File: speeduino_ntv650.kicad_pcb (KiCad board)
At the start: 2 copper layers, 0 parts

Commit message: first routing
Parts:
- added A1: Pololu_Breakout_A4988, ntv650_ecu:A4988 Stepper Motor Driver Carrier, B.Cu at (74.3, 77.5)
- added ARD1: ArduinoMegaProMini, ntv650_ecu:ArduinoMegaProMini, F.Cu at (117.0, 111.0)
- added C1: 0.01mF, Capacitors_ThroughHole:C_Axial_L5.1mm_D3.1mm_P7.50mm_Horizontal, B.Cu at (134.6, 86.4)
- added C10: 0.22uF, Capacitors_ThroughHole:C_Axial_L5.1mm_D3.1mm_P7.50mm_Horizontal, F.Cu at (109.0, 78.0)
- added C11: 0.1uF, Capacitors_ThroughHole:C_Axial_L5.1mm_D3.1mm_P7.50mm_Horizontal, B.Cu at (80.0, 57.8)
- added C12: 0.22uF, Capacitors_ThroughHole:C_Axial_L5.1mm_D3.1mm_P7.50mm_Horizontal, F.Cu at (121.9, 73.0)
- added C13: 0.1uF, Capacitors_ThroughHole:C_Axial_L5.1mm_D3.1mm_P7.50mm_Horizontal, F.Cu at (134.0, 97.0)
- added C14: 0.22uF, Capacitors_ThroughHole:C_Axial_L5.1mm_D3.1mm_P7.50mm_Horizontal, B.Cu at (140.3, 102.2)
- added C15: 0.1uF, Capacitors_ThroughHole:C_Axial_L5.1mm_D3.1mm_P7.50mm_Horizontal, F.Cu at (101.0, 58.4)
- added C16: 0.22uF, Capacitors_ThroughHole:C_Axial_L5.1mm_D3.1mm_P7.50mm_Horizontal, F.Cu at (117.0, 94.0)
- added C17: 1uF, Capacitors_ThroughHole:C_Axial_L5.1mm_D3.1mm_P7.50mm_Horizontal, F.Cu at (128.0, 38.0)
- added C18: 10uF, Capacitors_ThroughHole:C_Axial_L5.1mm_D3.1mm_P7.50mm_Horizontal, F.Cu at (85.0, 35.0)
- added C19: 0.1uF, Capacitors_ThroughHole:C_Axial_L5.1mm_D3.1mm_P7.50mm_Horizontal, F.Cu at (86.0, 50.0)
- added C2: 1nF, Capacitors_ThroughHole:C_Axial_L5.1mm_D3.1mm_P7.50mm_Horizontal, B.Cu at (151.8, 69.3)
- added C3: 1nF, Capacitors_ThroughHole:C_Axial_L5.1mm_D3.1mm_P7.50mm_Horizontal, F.Cu at (151.8, 88.3)
- added C4: 0.3uF, Capacitors_ThroughHole:C_Axial_L5.1mm_D3.1mm_P7.50mm_Horizontal, F.Cu at (134.0, 54.0)
- added C5: 1uF, Capacitors_ThroughHole:C_Axial_L5.1mm_D3.1mm_P7.50mm_Horizontal, F.Cu at (121.3, 58.4)
- added C6: 0.01uF, Capacitors_ThroughHole:C_Axial_L5.1mm_D3.1mm_P7.50mm_Horizontal, F.Cu at (128.3, 58.4)
- added C7: 0.1uF, Capacitors_ThroughHole:C_Axial_L5.1mm_D3.1mm_P7.50mm_Horizontal, F.Cu at (111.8, 58.4)
- added C8: 0.22uF, Capacitors_ThroughHole:C_Axial_L5.1mm_D3.1mm_P7.50mm_Horizontal, F.Cu at (117.0, 88.0)
- added C9: 0.1uF, Capacitors_ThroughHole:C_Axial_L5.1mm_D3.1mm_P7.50mm_Horizontal, F.Cu at (94.6, 58.4)
- added D1: LED, LEDs:LED_0805, F.Cu at (141.6, 18.4)
- added D2: D, Diodes_SMD:D_0805, F.Cu at (79.4, 17.1)
- added D3: LED, LEDs:LED_0805, F.Cu at (149.0, 35.0)
- added D4: D, Diodes_SMD:D_0805, F.Cu at (146.0, 28.0)
- added D5: LED, LEDs:LED_0805, F.Cu at (133.0, 73.0)
- added D6: LED, LEDs:LED_0805, F.Cu at (104.0, 95.0)
- added D7: 1N5818, Diodes_ThroughHole:D_DO-15_P12.70mm_Horizontal, F.Cu at (69.2, 33.7)
- added D8: 1N5919BG, Diodes_ThroughHole:D_DO-15_P12.70mm_Horizontal, F.Cu at (102.2, 71.8)
- added IC1: SP721, Housings_SOIC:SOIC-8-1EP_3.9x4.9mm_Pitch1.27mm, F.Cu at (111.7, 92.0)
- added IC2: TC4424, Housings_SOIC:SOIC-16W_7.5x10.3mm_Pitch1.27mm, F.Cu at (120.0, 39.0)
- added J1: Conn_01x25_DB-25, ntv650_ecu:DSUB-25_Male_Horizontal_P2.77x2.84mm_EdgePinOffset9.90mm_Housed_MountingHolesOffset11.32mm, F.Cu at (127.0, 27.9)
- added P1: MAX9926_9927, Housings_SSOP:QSOP-16_3.9x4.9mm_Pitch0.635mm, F.Cu at (144.8, 73.7)
- added Q1: STP62NS04Z, TO_SOT_Packages_THT:TO-220-3_Vertical, F.Cu at (104.8, 41.9)
- added Q2: STP62NS04Z, TO_SOT_Packages_THT:TO-220-3_Vertical, F.Cu at (98.4, 42.5)
- added Q3: STP62NS04Z, TO_SOT_Packages_THT:TO-220-3_Vertical, F.Cu at (72.4, 43.8)
- added R1: 1k, Resistors_SMD:R_0805, F.Cu at (106.0, 64.8)
- added R10: 2.49K, Resistors_SMD:R_0805, F.Cu at (88.3, 59.1)
- added R11: 470, Resistors_SMD:R_0805, F.Cu at (88.0, 63.0)
- added R12: 3.9K, Resistors_SMD:R_0805, F.Cu at (128.0, 97.0)
- added R13: 1K, Resistors_SMD:R_0805, F.Cu at (141.0, 98.0)
- added R14: 470, Resistors_SMD:R_0805, F.Cu at (136.0, 101.0)
- added R15: 2.49K, Resistors_SMD:R_0805, F.Cu at (106.0, 59.1)
- added R16: 470, Resistors_SMD:R_0805, F.Cu at (109.0, 71.0)
- added R17: 2.4K, Resistors_SMD:R_0805, F.Cu at (140.0, 34.0)
- added R18: 100K, Resistors_SMD:R_0805, F.Cu at (97.0, 92.0)
- added R19: 1K, Resistors_SMD:R_0805, F.Cu at (104.0, 51.0)
- added R2: 1k, Resistors_SMD:R_0805, F.Cu at (86.0, 95.0)
- added R20: 2.4K, Resistors_SMD:R_0805, F.Cu at (145.0, 34.0)
- added R21: 100K, Resistors_SMD:R_0805, F.Cu at (92.0, 95.0)
- added R22: 1K, Resistors_SMD:R_0805, F.Cu at (99.0, 55.0)
- added R23: 1K, Resistors_SMD:R_0805, F.Cu at (99.0, 49.0)
- added R24: 1K, Resistors_SMD:R_0805, F.Cu at (109.0, 52.0)
- added R25: 100K, Resistors_SMD:R_0805, F.Cu at (129.0, 44.0)
- added R26: 100K, Resistors_SMD:R_0805, F.Cu at (126.0, 48.0)
- added R27: 2.4K, Resistors_SMD:R_0805, F.Cu at (116.0, 69.0)
- added R28: 2.4K, Resistors_SMD:R_0805, F.Cu at (104.0, 55.0)
- added R29: 160, Resistors_SMD:R_0805, F.Cu at (106.0, 34.0)
- added R3: 10k, Resistors_SMD:R_0805, F.Cu at (150.5, 58.7)
- added R30: 160, Resistors_SMD:R_0805, F.Cu at (110.0, 35.0)
- added R31: 100K, Resistors_SMD:R_0805, B.Cu at (104.0, 95.0)
- added R32: 1K, Resistors_SMD:R_0805, F.Cu at (83.0, 88.0)
- added R4: 10k, Resistors_SMD:R_0805, F.Cu at (146.1, 58.7)
- added R5: 10k, Resistors_SMD:R_0805, F.Cu at (137.8, 59.1)
- added R6: 10k, Resistors_SMD:R_0805, F.Cu at (141.6, 58.7)
- added R7: 750, Resistors_SMD:R_0805, F.Cu at (132.7, 58.7)
- added R8: 470, Resistors_SMD:R_0805, F.Cu at (116.8, 58.7)
- added R9: 470, Resistors_SMD:R_0805, F.Cu at (96.0, 74.0)
- added RV1: ERZV14D220, Varistors:RV_Disc_D12_W3.9_P7.5, F.Cu at (78.1, 25.4)
- added U1: LM2937xT, TO_SOT_Packages_THT:TO-220-3_Vertical, F.Cu at (69.2, 17.8)
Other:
- board outline added: 87.6 x 123.8 mm

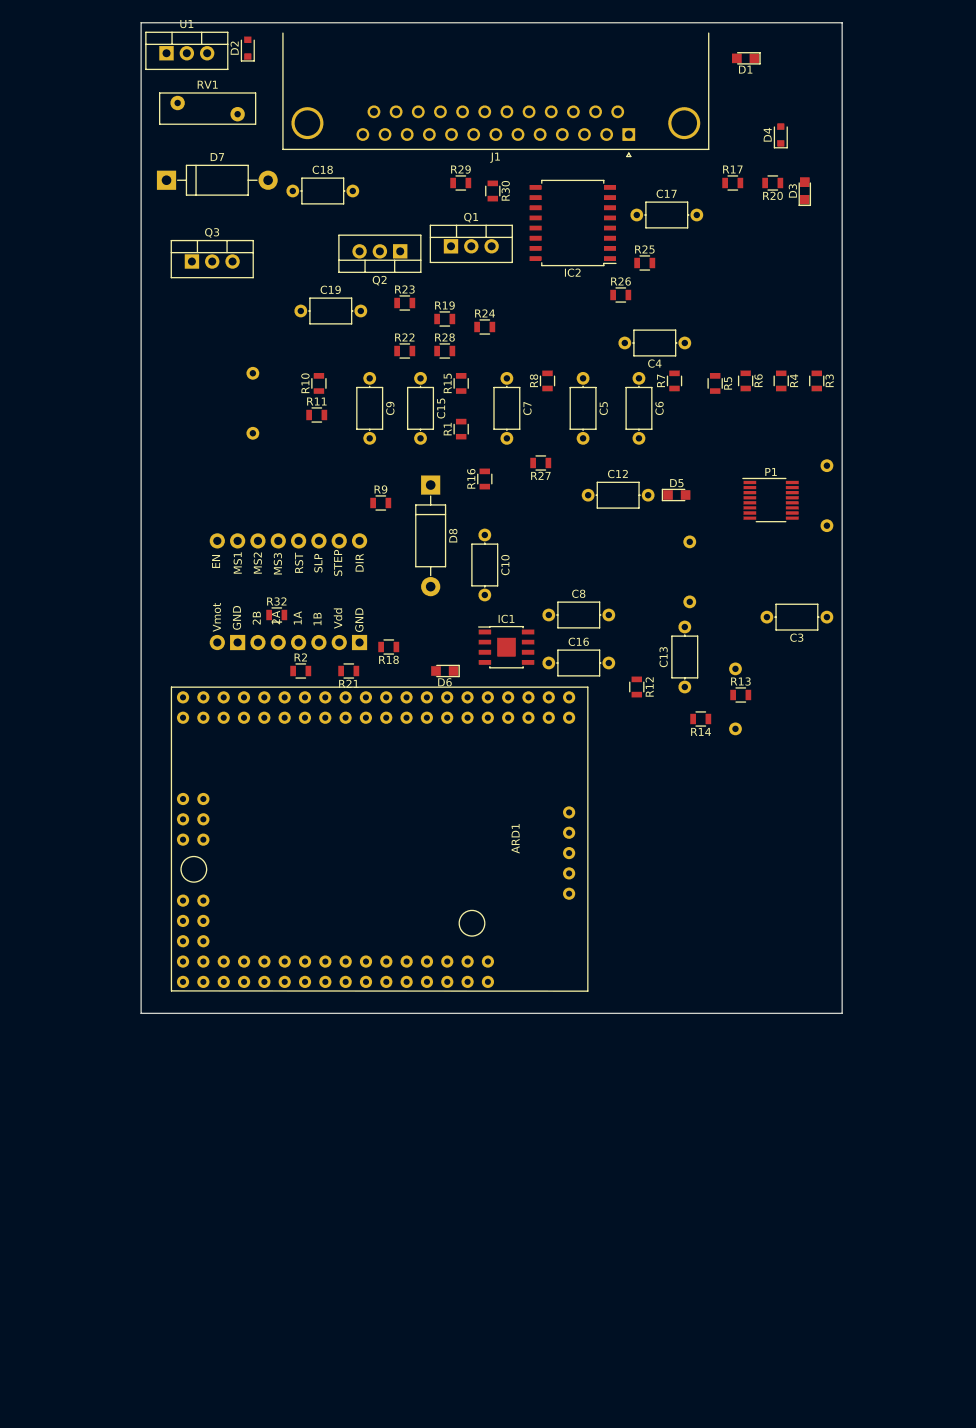
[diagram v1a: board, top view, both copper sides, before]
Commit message: add net classes
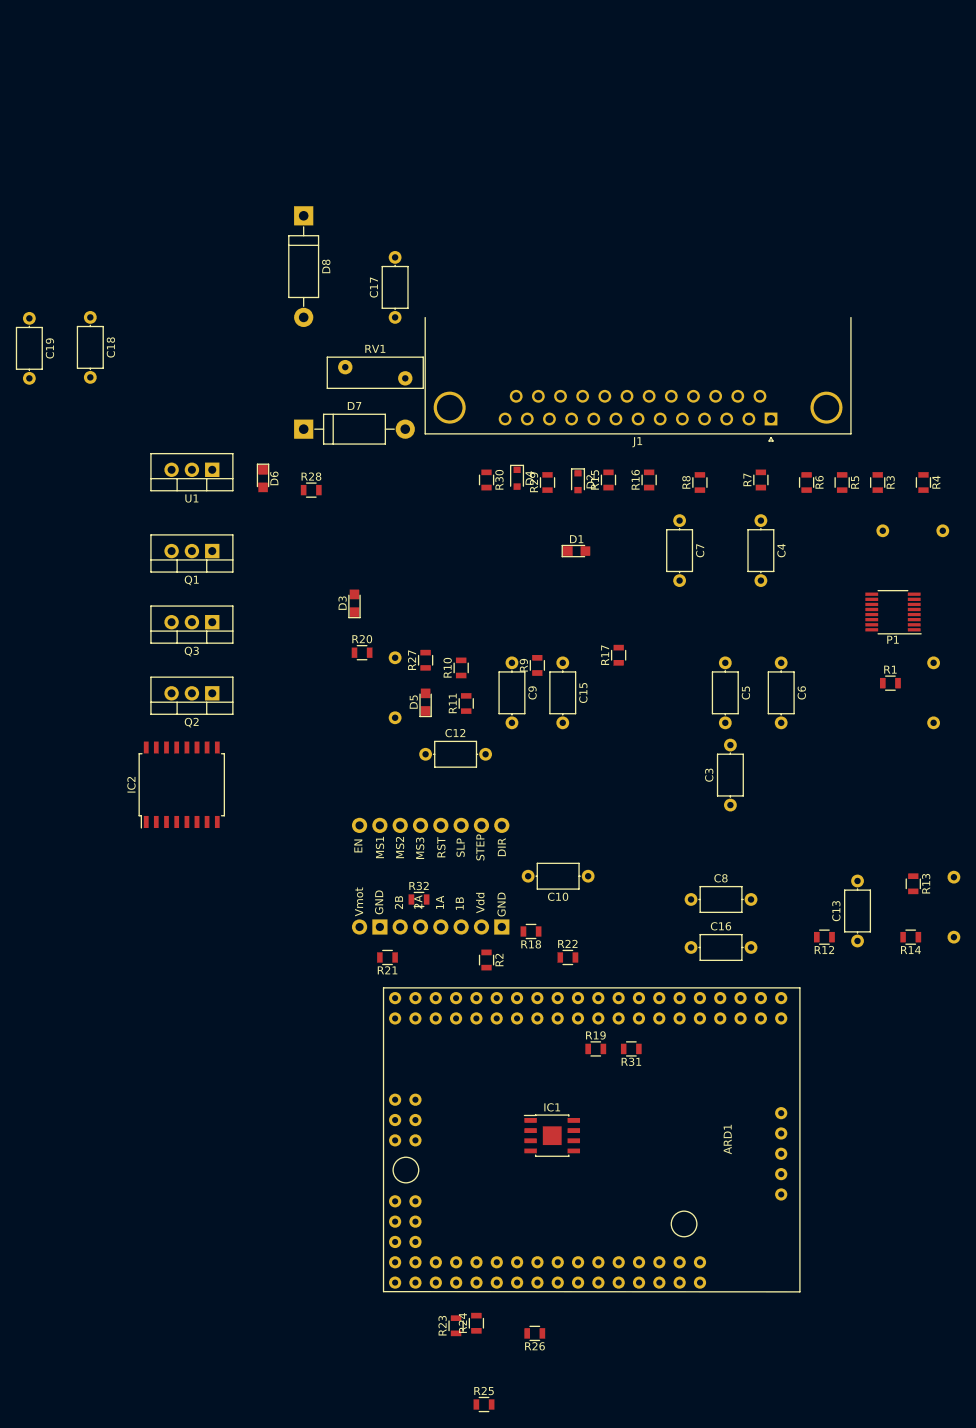
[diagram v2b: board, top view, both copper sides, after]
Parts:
- R31: moved to F.Cu
- moved R25 144.1 mm to (108.9, 186.7)
- moved R26 130.2 mm to (115.2, 177.8), turned to 180 degrees
- moved R23 128.0 mm to (105.4, 176.8), turned to 90 degrees
- moved R24 124.5 mm to (108.0, 176.5), turned to 90 degrees
- moved R19 93.2 mm to (122.9, 142.2)
- moved IC2 85.6 mm to (71.1, 109.2), turned to 90 degrees
- moved R22 78.5 mm to (119.4, 130.8)
- moved R20 78.0 mm to (93.7, 92.7), turned to 0 degrees
- moved D3 76.3 mm to (92.7, 86.5)
- moved D2 68.1 mm to (120.7, 71.3), turned to 270 degrees
- moved D1 65.1 mm to (120.5, 80.0), turned to 0 degrees
- moved R1 62.3 mm to (159.7, 96.5), turned to 0 degrees
- moved IC1 61.3 mm to (117.4, 153.1)
- moved R17 60.7 mm to (125.7, 93.0), turned to 90 degrees
- moved Q2 60.0 mm to (74.9, 97.8)
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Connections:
- A1 pad 10: (no net) -> Net-(A1-Pad10)
- A1 pad 11: (no net) -> Net-(A1-Pad11)
- A1 pad 12: (no net) -> Net-(A1-Pad12)
- ARD1 pad 0: (no net) -> Net-(ARD1-Pad0)
- ARD1 pad 1: (no net) -> Net-(ARD1-Pad1)
- ARD1 pad 10: (no net) -> Net-(ARD1-Pad10)
- ARD1 pad 11: (no net) -> Net-(ARD1-Pad11)
- ARD1 pad 12: (no net) -> Net-(ARD1-Pad12)
- ARD1 pad 13: (no net) -> Net-(ARD1-Pad13)
- ARD1 pad 14: (no net) -> Net-(ARD1-Pad14)
- ARD1 pad 15: (no net) -> Net-(ARD1-Pad15)
- ARD1 pad 2: (no net) -> Net-(ARD1-Pad2)
- ARD1 pad 20: (no net) -> Net-(ARD1-Pad20)
- ARD1 pad 21: (no net) -> Net-(ARD1-Pad21)
- ARD1 pad 22: (no net) -> Net-(ARD1-Pad22)
- ARD1 pad 23: (no net) -> Net-(ARD1-Pad23)
- ARD1 pad 25: (no net) -> Net-(ARD1-Pad25)
- ARD1 pad 26: (no net) -> Net-(ARD1-Pad26)
- ARD1 pad 27: (no net) -> Net-(ARD1-Pad27)
- ARD1 pad 28: (no net) -> Net-(ARD1-Pad28)
- ARD1 pad 29: (no net) -> Net-(ARD1-Pad29)
- ARD1 pad 3: (no net) -> Net-(ARD1-Pad3)
- ARD1 pad 30: (no net) -> Net-(ARD1-Pad30)
- ARD1 pad 31: (no net) -> Net-(ARD1-Pad31)
- ARD1 pad 32: (no net) -> Net-(ARD1-Pad32)
- ARD1 pad 33: (no net) -> Net-(ARD1-Pad33)
- ARD1 pad 34: (no net) -> Net-(ARD1-Pad34)
- ARD1 pad 35: (no net) -> Net-(ARD1-Pad35)
- ARD1 pad 36: (no net) -> Net-(ARD1-Pad36)
- ARD1 pad 37: (no net) -> Net-(ARD1-Pad37)
- ARD1 pad 39: (no net) -> Net-(ARD1-Pad39)
- ARD1 pad 4: (no net) -> Net-(ARD1-Pad4)
- ARD1 pad 41: (no net) -> Net-(ARD1-Pad41)
- ARD1 pad 42: (no net) -> Net-(ARD1-Pad42)
- ARD1 pad 43: (no net) -> Net-(ARD1-Pad43)
- ARD1 pad 44: (no net) -> Net-(ARD1-Pad44)
- ARD1 pad 45: (no net) -> Net-(ARD1-Pad45)
- ARD1 pad 46: (no net) -> Net-(ARD1-Pad46)
- ARD1 pad 47: (no net) -> Net-(ARD1-Pad47)
- ARD1 pad 48: (no net) -> Net-(ARD1-Pad48)
- ARD1 pad 49: (no net) -> Net-(ARD1-Pad49)
- ARD1 pad 5: (no net) -> Net-(ARD1-Pad5)
- ARD1 pad 50: (no net) -> Net-(ARD1-Pad50)
- ARD1 pad 51: (no net) -> Net-(ARD1-Pad51)
- ARD1 pad 52: (no net) -> Net-(ARD1-Pad52)
- ARD1 pad 53: (no net) -> Net-(ARD1-Pad53)
- ARD1 pad 59: (no net) -> Net-(ARD1-Pad59)
- ARD1 pad 60: (no net) -> Net-(ARD1-Pad60)
- ARD1 pad 61: (no net) -> Net-(ARD1-Pad61)
- ARD1 pad 63: (no net) -> Net-(ARD1-Pad63)
- ARD1 pad 64: (no net) -> Net-(ARD1-Pad64)
- ARD1 pad 65: (no net) -> Net-(ARD1-Pad65)
- ARD1 pad 66: (no net) -> Net-(ARD1-Pad66)
- ARD1 pad 67: (no net) -> Net-(ARD1-Pad67)
- ARD1 pad 68: (no net) -> Net-(ARD1-Pad68)
- ARD1 pad 69: (no net) -> Net-(ARD1-Pad69)
- ARD1 pad 7: (no net) -> Net-(ARD1-Pad7)
- ARD1 pad 70: (no net) -> Net-(ARD1-Pad70)
- ARD1 pad 71: (no net) -> Net-(ARD1-Pad71)
- ARD1 pad 72: (no net) -> Net-(ARD1-Pad72)
- ARD1 pad 73: (no net) -> Net-(ARD1-Pad73)
- ARD1 pad 74: (no net) -> Net-(ARD1-Pad74)
- ARD1 pad 75: (no net) -> Net-(ARD1-Pad75)
- ARD1 pad 76: (no net) -> Net-(ARD1-Pad76)
- ARD1 pad 77: (no net) -> Net-(ARD1-Pad77)
- ARD1 pad 78: (no net) -> Net-(ARD1-Pad78)
- ARD1 pad 79: (no net) -> Net-(ARD1-Pad79)
- ARD1 pad 82: (no net) -> Net-(ARD1-Pad82)
- ARD1 pad 83: (no net) -> Net-(ARD1-Pad83)
- ARD1 pad 84: (no net) -> Net-(ARD1-Pad84)
- ARD1 pad 85: (no net) -> Net-(ARD1-Pad85)
- ARD1 pad 86: (no net) -> Net-(ARD1-Pad86)
- IC2 pad 1: (no net) -> Net-(IC2-Pad1)
- IC2 pad 8: (no net) -> Net-(IC2-Pad8)
- J1 pad 10: (no net) -> Net-(J1-Pad10)
- J1 pad 12: (no net) -> Net-(J1-Pad12)
- J1 pad 23: (no net) -> Net-(J1-Pad23)
- J1 pad 24: (no net) -> Net-(J1-Pad24)
- J1 pad 25: (no net) -> Net-(J1-Pad25)
- P1 pad 12: (no net) -> Net-(P1-Pad12)
- P1 pad 2: (no net) -> Net-(P1-Pad2)
- P1 pad 7: (no net) -> Net-(P1-Pad7)
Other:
- board outline removed
- net class Default: clearance 0.2 -> 0.3; trace_width 0.25 -> 0.4
- net class POWER_ENG added: clearance 0.6, trace_width 0.8, via_dia 0.8, via_drill 0.4
- net class Power added: clearance 0.6, trace_width 0.8, via_dia 1, via_drill 0.6
- net class power_exit added: clearance 0.8, trace_width 1, via_dia 0.8, via_drill 0.4
- net class step_engine_exit added: clearance 0.4, trace_width 0.6, via_dia 0.8, via_drill 0.4
- rule trace_clearance: 0.2 -> 0.3

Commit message: second routs
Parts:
- D1, D3: value LED -> LED INJ
- D5: value LED -> LED AGN2
- D6: value LED -> LED AGN1
- D7, D8: footprint Diodes_ThroughHole:D_DO-15_P12.70mm_Horizontal -> Diodes_ThroughHole:D_DO-41_SOD81_P7.62mm_Horizontal
- IC2: footprint Housings_SOIC:SOIC-16W_7.5x10.3mm_Pitch1.27mm -> Housings_SOIC:SOIC-8_3.9x4.9mm_Pitch1.27mm
- R10, R11, R12, R13, R14, R15, R18, R19, R21, R22, R3, R31, R32, R4, R5, R6, R7, R9: moved to B.Cu
- moved R12 119.4 mm to (82.9, 30.5), turned to 0 degrees
- moved R13 117.3 mm to (82.9, 35.6), turned to 0 degrees
- moved R26 92.5 mm to (154.9, 94.3), turned to 270 degrees
- moved R31 91.9 mm to (85.7, 60.3)
- moved R25 91.6 mm to (150.5, 105.1), turned to 90 degrees
- moved R24 90.9 mm to (154.9, 98.7), turned to 270 degrees
- moved ARD1 88.0 mm to (98.4, 73.0), turned to 0 degrees
- moved R23 82.5 mm to (146.1, 105.1), turned to 270 degrees
- moved IC2 77.1 mm to (147.3, 97.2)
- moved R21 75.1 mm to (85.7, 56.5)
- moved C16 69.3 mm to (115.7, 62.9)
- moved C8 69.3 mm to (115.7, 56.9)
- moved R19 65.7 mm to (144.8, 80.3), turned to 270 degrees
- moved R32 64.9 mm to (144.8, 75.9), turned to 270 degrees
- moved C12 63.1 mm to (160.7, 83.2), turned to 90 degrees
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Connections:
- A1 pad 10: Net-(A1-Pad10) -> (no net)
- A1 pad 11: Net-(A1-Pad11) -> (no net)
- A1 pad 12: Net-(A1-Pad12) -> (no net)
- ARD1 pad 0: Net-(ARD1-Pad0) -> (no net)
- ARD1 pad 1: Net-(ARD1-Pad1) -> (no net)
- ARD1 pad 10: Net-(ARD1-Pad10) -> (no net)
- ARD1 pad 11: Net-(ARD1-Pad11) -> (no net)
- ARD1 pad 12: Net-(ARD1-Pad12) -> (no net)
- ARD1 pad 13: Net-(ARD1-Pad13) -> (no net)
- ARD1 pad 14: Net-(ARD1-Pad14) -> (no net)
- ARD1 pad 15: Net-(ARD1-Pad15) -> (no net)
- ARD1 pad 2: Net-(ARD1-Pad2) -> (no net)
- ARD1 pad 20: Net-(ARD1-Pad20) -> (no net)
- ARD1 pad 21: Net-(ARD1-Pad21) -> (no net)
- ARD1 pad 22: Net-(ARD1-Pad22) -> (no net)
- ARD1 pad 23: Net-(ARD1-Pad23) -> (no net)
- ARD1 pad 25: Net-(ARD1-Pad25) -> (no net)
- ARD1 pad 26: Net-(ARD1-Pad26) -> (no net)
- ARD1 pad 27: Net-(ARD1-Pad27) -> (no net)
- ARD1 pad 28: Net-(ARD1-Pad28) -> (no net)
- ARD1 pad 29: Net-(ARD1-Pad29) -> (no net)
- ARD1 pad 3: Net-(ARD1-Pad3) -> (no net)
- ARD1 pad 30: Net-(ARD1-Pad30) -> (no net)
- ARD1 pad 31: Net-(ARD1-Pad31) -> (no net)
- ARD1 pad 32: Net-(ARD1-Pad32) -> (no net)
- ARD1 pad 33: Net-(ARD1-Pad33) -> (no net)
- ARD1 pad 34: Net-(ARD1-Pad34) -> (no net)
- ARD1 pad 35: Net-(ARD1-Pad35) -> (no net)
- ARD1 pad 36: Net-(ARD1-Pad36) -> (no net)
- ARD1 pad 37: Net-(ARD1-Pad37) -> (no net)
- ARD1 pad 39: Net-(ARD1-Pad39) -> (no net)
- ARD1 pad 4: Net-(ARD1-Pad4) -> (no net)
- ARD1 pad 41: Net-(ARD1-Pad41) -> (no net)
- ARD1 pad 42: Net-(ARD1-Pad42) -> (no net)
- ARD1 pad 43: Net-(ARD1-Pad43) -> (no net)
- ARD1 pad 44: Net-(ARD1-Pad44) -> (no net)
- ARD1 pad 45: Net-(ARD1-Pad45) -> (no net)
- ARD1 pad 46: Net-(ARD1-Pad46) -> (no net)
- ARD1 pad 47: Net-(ARD1-Pad47) -> (no net)
- ARD1 pad 48: Net-(ARD1-Pad48) -> (no net)
- ARD1 pad 49: Net-(ARD1-Pad49) -> (no net)
- ARD1 pad 5: Net-(ARD1-Pad5) -> (no net)
- ARD1 pad 50: Net-(ARD1-Pad50) -> (no net)
- ARD1 pad 51: Net-(ARD1-Pad51) -> (no net)
- ARD1 pad 52: Net-(ARD1-Pad52) -> (no net)
- ARD1 pad 53: Net-(ARD1-Pad53) -> (no net)
- ARD1 pad 59: Net-(ARD1-Pad59) -> (no net)
- ARD1 pad 60: Net-(ARD1-Pad60) -> (no net)
- ARD1 pad 61: Net-(ARD1-Pad61) -> (no net)
- ARD1 pad 63: Net-(ARD1-Pad63) -> (no net)
- ARD1 pad 64: Net-(ARD1-Pad64) -> (no net)
- ARD1 pad 65: Net-(ARD1-Pad65) -> (no net)
- ARD1 pad 66: Net-(ARD1-Pad66) -> (no net)
- ARD1 pad 67: Net-(ARD1-Pad67) -> (no net)
- ARD1 pad 68: Net-(ARD1-Pad68) -> (no net)
- ARD1 pad 69: Net-(ARD1-Pad69) -> (no net)
- ARD1 pad 7: Net-(ARD1-Pad7) -> (no net)
- ARD1 pad 70: Net-(ARD1-Pad70) -> (no net)
- ARD1 pad 71: Net-(ARD1-Pad71) -> (no net)
- ARD1 pad 72: Net-(ARD1-Pad72) -> (no net)
- ARD1 pad 73: Net-(ARD1-Pad73) -> (no net)
- ARD1 pad 74: Net-(ARD1-Pad74) -> (no net)
- ARD1 pad 75: Net-(ARD1-Pad75) -> (no net)
- ARD1 pad 76: Net-(ARD1-Pad76) -> (no net)
- ARD1 pad 77: Net-(ARD1-Pad77) -> (no net)
- ARD1 pad 78: Net-(ARD1-Pad78) -> (no net)
- ARD1 pad 79: Net-(ARD1-Pad79) -> (no net)
- ARD1 pad 82: Net-(ARD1-Pad82) -> (no net)
- ARD1 pad 83: Net-(ARD1-Pad83) -> (no net)
- ARD1 pad 84: Net-(ARD1-Pad84) -> (no net)
- ARD1 pad 85: Net-(ARD1-Pad85) -> (no net)
- ARD1 pad 86: Net-(ARD1-Pad86) -> (no net)
- IC2 pad 1: Net-(IC2-Pad1) -> (no net)
- IC2 pad 8: Net-(IC2-Pad8) -> (no net)
- J1 pad 10: Net-(J1-Pad10) -> (no net)
- J1 pad 12: Net-(J1-Pad12) -> 12V
- J1 pad 13: 12V -> GND
- J1 pad 23: Net-(J1-Pad23) -> (no net)
- J1 pad 24: Net-(J1-Pad24) -> 12V
- J1 pad 25: Net-(J1-Pad25) -> GND
- P1 pad 12: Net-(P1-Pad12) -> (no net)
- P1 pad 2: Net-(P1-Pad2) -> (no net)
- P1 pad 7: Net-(P1-Pad7) -> (no net)
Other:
- board outline added: 101.6 x 96.5 mm
- net class GND_MOSFIT added: clearance 0.3, trace_width 0.6, via_dia 1, via_drill 0.8
- net class POWER_ENG: clearance 0.6 -> 0.4
- net class Power: clearance 0.6 -> 0.4
- net class power_exit: clearance 0.8 -> 0.4
- net class power_logic added: clearance 0.3, trace_width 0.4, via_dia 0.8, via_drill 0.7

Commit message: attempt
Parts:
- R12, R13: moved to F.Cu
- moved D5 70.5 mm to (155.1, 31.8), turned to 180 degrees
- moved R14 68.7 mm to (92.4, 56.5), turned to 0 degrees
- moved D6 67.4 mm to (155.1, 36.8), turned to 180 degrees
- moved R32 65.0 mm to (80.0, 70.2)
- moved R22 64.3 mm to (80.6, 89.5)
- moved D3 64.2 mm to (77.5, 109.7)
- moved D4 64.2 mm to (77.5, 114.7)
- moved R20 64.2 mm to (77.5, 105.1)
- moved D2 64.2 mm to (72.4, 114.7)
- moved D1 64.2 mm to (72.4, 110.3)
- moved R17 64.2 mm to (72.4, 105.1)
- moved R19 64.1 mm to (80.6, 79.4)
- moved R27 62.9 mm to (148.9, 31.8), turned to 180 degrees
- moved R28 60.3 mm to (149.5, 36.8), turned to 180 degrees
- moved C13 59.7 mm to (103.5, 55.9)
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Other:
- net class Default: clearance 0.3 -> 0.4
- net class GND_MOSFIT: clearance 0.3 -> 0.4
- rule trace_clearance: 0.3 -> 0.4
